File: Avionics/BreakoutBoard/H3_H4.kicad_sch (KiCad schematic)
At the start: 2 parts

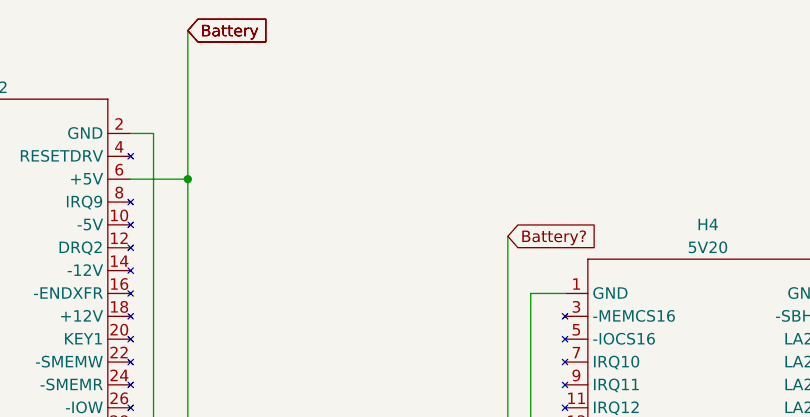
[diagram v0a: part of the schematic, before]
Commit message: Sephora Poteau: Added changes to schema and pcb
Added 3V3 voltage indicator for power recieved by PCB and BOB has been appropriately traced and filled with copper
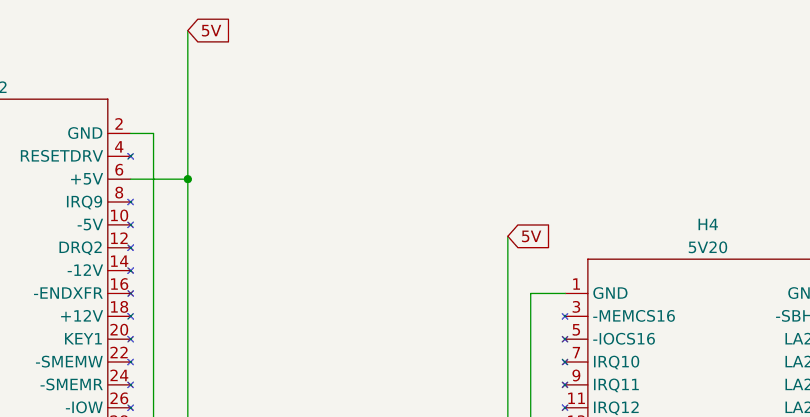
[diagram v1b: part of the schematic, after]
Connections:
- net Battery? is gone; now on net 5V: H4.33 (+5V)
- net Battery renamed 5V
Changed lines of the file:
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@@
 		)
 	)
-	(global_label "Battery?"
+	(global_label "5V"
 		(shape input)
 		(at 165.1 57.15 0)
@@
 		)
 		(property "Intersheetrefs" "${INTERSHEET_REFS}"
-			(at 175.8866 57.15 0)
+			(at 170.3833 57.15 0)
 			(effects
 				(font
@@
 		)
 	)
-	(global_label "Battery"
+	(global_label "5V"
 		(shape input)
 		(at 129.54 34.29 0)
@@
 		)
 		(property "Intersheetrefs" "${INTERSHEET_REFS}"
-			(at 139.238 34.29 0)
+			(at 134.8233 34.29 0)
 			(effects
 				(font
-					(size 1.27 1.27)
-				)
-				(justify left)
-				(hide yes)
-			)
-		)
-	)
-	(global_label "Battery"
-		(shape input)
-		(at 129.54 34.29 0)
-		(fields_autoplaced yes)
-		(effects
-			(font
-				(size 1.27 1.27)
-			)
-			(justify left)
-		)
-		(property "Intersheetrefs" "${INTERSHEET_REFS}"
-			(at 139.238 34.29 0)
-			(effects
-				(font
